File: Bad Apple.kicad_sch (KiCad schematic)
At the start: 0 parts

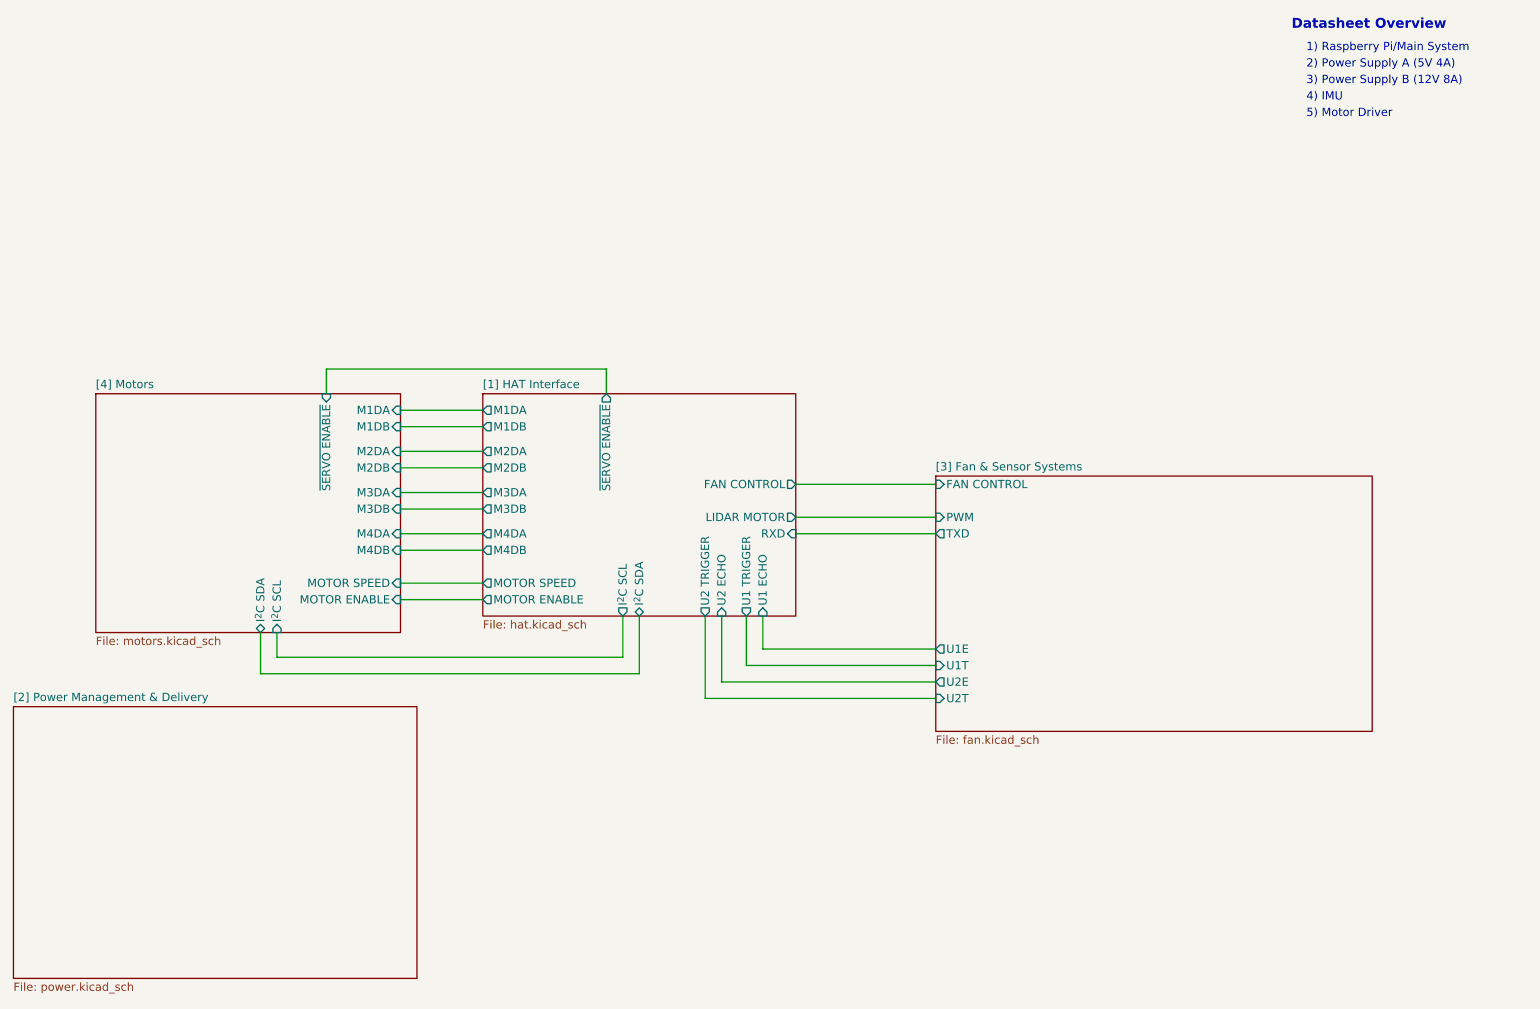
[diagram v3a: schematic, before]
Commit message: feat(pcb): (somewhat) finalized all the parts needed
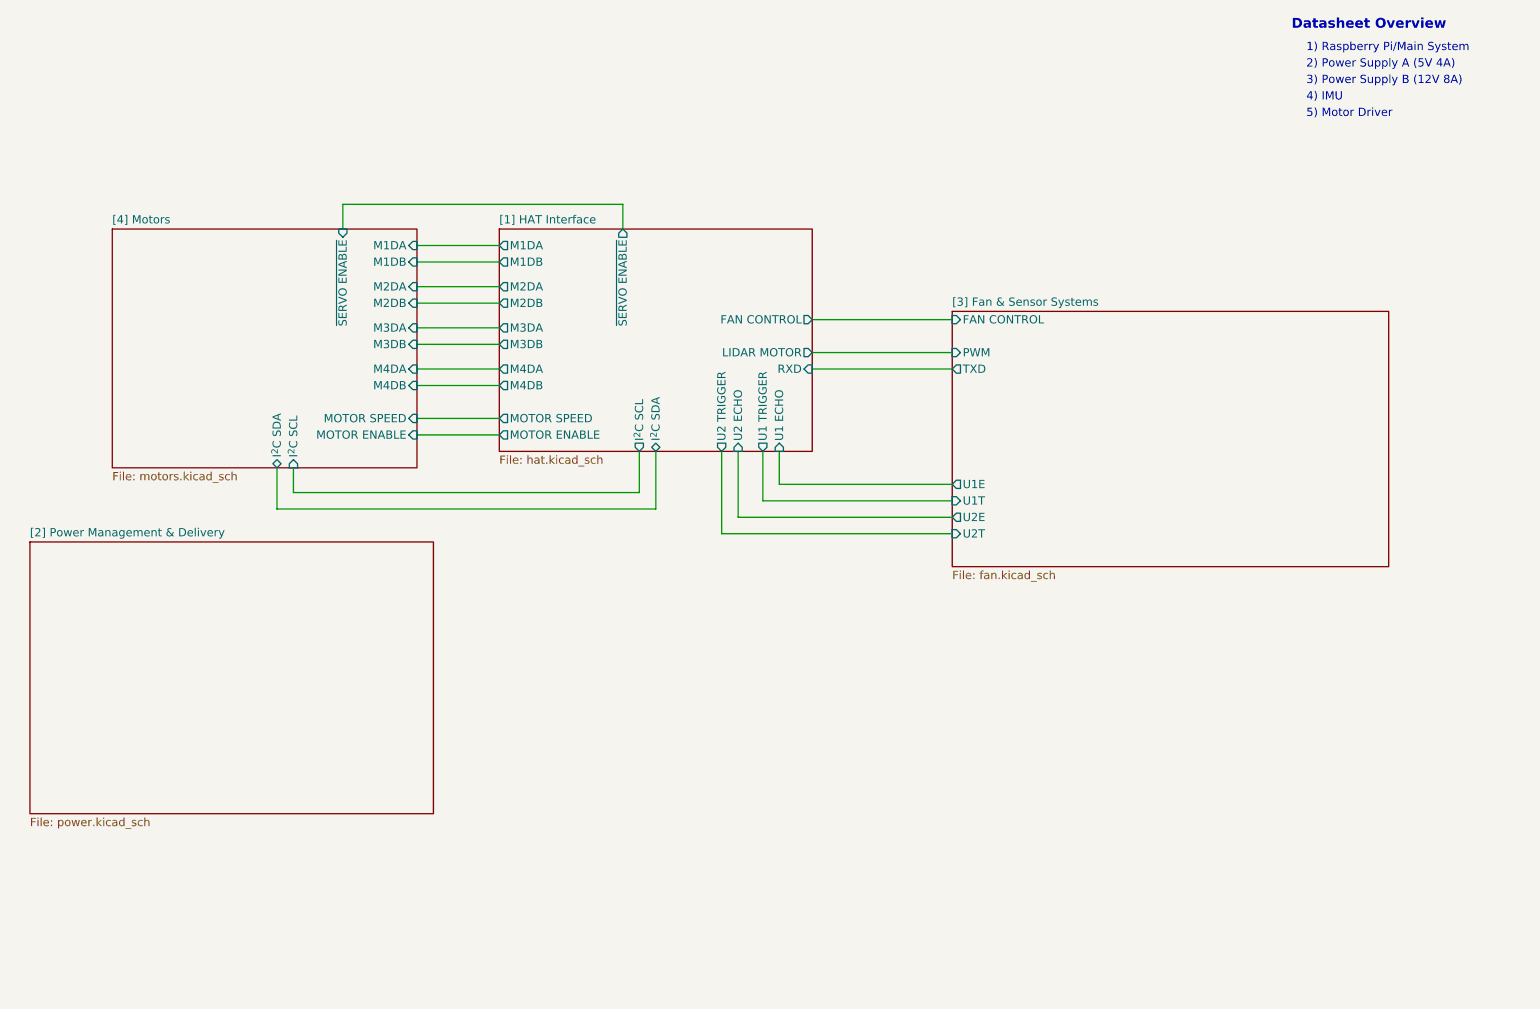
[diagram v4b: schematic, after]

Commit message: feat: cleared the PCB design for a much better thingy
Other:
- sheet [3] Fan & Sensor Systems ports: added I^{2}C SCL, I^{2}C SDA; removed none
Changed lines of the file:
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@@
+		)
+	)
+	(junction
+		(at 137.16 87.63)
+		(diameter 0)
+		(color 0 0 0 0)
+	)
+	(junction
+		(at 139.7 90.17)
+		(diameter 0)
+		(color 0 0 0 0)
+	)
+	(wire
+		(pts
+			(xy 212.09 99.06) (xy 212.09 107.95)
+		)
+		(stroke
+			(width 0)
+			(type default)
 		)
 	)
@@
 	(wire
 		(pts
+			(xy 209.55 105.41) (xy 139.7 105.41)
+		)
+		(stroke
+			(width 0)
+			(type default)
+		)
+	)
+	(wire
+		(pts
 			(xy 158.75 81.28) (xy 158.75 86.36)
 		)
@@
 	(wire
 		(pts
+			(xy 139.7 90.17) (xy 139.7 105.41)
+		)
+		(stroke
+			(width 0)
+			(type default)
+		)
+	)
+	(wire
+		(pts
+			(xy 212.09 107.95) (xy 137.16 107.95)
+		)
+		(stroke
+			(width 0)
+			(type default)
+		)
+	)
+	(wire
+		(pts
 			(xy 163.83 66.04) (xy 185.42 66.04)
 		)
@@
 	(wire
 		(pts
+			(xy 209.55 99.06) (xy 209.55 105.41)
+		)
+		(stroke
+			(width 0)
+			(type default)
+		)
+	)
+	(wire
+		(pts
 			(xy 102.87 49.53) (xy 115.57 49.53)
 		)
@@
 		(pts
 			(xy 102.87 64.77) (xy 115.57 64.77)
+		)
+		(stroke
+			(width 0)
+			(type default)
+		)
+	)
+	(wire
+		(pts
+			(xy 137.16 87.63) (xy 137.16 107.95)
 		)
 		(stroke
@@
 			(effects
 				(font
+					(size 1.27 1.27)
+				)
+				(justify left)
+			)
+		)
+		(pin "I^{2}C SCL" input
+			(at 212.09 99.06 270)
+			(effects
+				(font
+					(size 1.27 1.27)
+				)
+				(justify left)
+			)
+		)
+		(pin "I^{2}C SDA" bidirectional
+			(at 209.55 99.06 270)
+			(effects
+				(font

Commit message: feat: (hopefully) gave connections to everything else
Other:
- sheet [1] HAT Interface ports: added AUDIO CLK, AUDIO FRAME, AUDIO IN, AUDIO OUT; removed none
- sheet [3] Fan & Sensor Systems ports: added AUDIO CLK, AUDIO FRAME, AUDIO IN, AUDIO OUT; removed none
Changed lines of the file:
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@@
+	(wire
+		(pts
+			(xy 215.9 57.15) (xy 215.9 59.69)
+		)
+		(stroke
+			(width 0)
+			(type default)
+		)
+	)
 	(wire
 		(pts
@@
 	(wire
 		(pts
+			(xy 163.83 49.53) (xy 223.52 49.53)
+		)
+		(stroke
+			(width 0)
+			(type default)
+		)
+	)
+	(wire
+		(pts
+			(xy 220.98 59.69) (xy 220.98 52.07)
+		)
+		(stroke
+			(width 0)
+			(type default)
+		)
+	)
+	(wire
+		(pts
+			(xy 223.52 49.53) (xy 223.52 59.69)
+		)
+		(stroke
+			(width 0)
+			(type default)
+		)
+	)
+	(wire
+		(pts
+			(xy 163.83 57.15) (xy 215.9 57.15)
+		)
+		(stroke
+			(width 0)
+			(type default)
+		)
+	)
+	(wire
+		(pts
 			(xy 212.09 107.95) (xy 137.16 107.95)
 		)
@@
 	(wire
 		(pts
+			(xy 218.44 54.61) (xy 218.44 59.69)
+		)
+		(stroke
+			(width 0)
+			(type default)
+		)
+	)
+	(wire
+		(pts
 			(xy 91.44 46.99) (xy 91.44 43.18)
 		)
@@
 		(pts
 			(xy 156.21 81.28) (xy 156.21 88.9)
+		)
+		(stroke
+			(width 0)
+			(type default)
+		)
+	)
+	(wire
+		(pts
+			(xy 163.83 54.61) (xy 218.44 54.61)
+		)
+		(stroke
+			(width 0)
+			(type default)
+		)
+	)
+	(wire
+		(pts
+			(xy 220.98 52.07) (xy 163.83 52.07)
 		)
 		(stroke
@@
 			)
 		)
+		(pin "AUDIO CLK" output
+			(at 163.83 49.53 0)
+			(effects
+				(font
+					(size 1.27 1.27)
+				)
+				(justify right)
+			)
+		)
+		(pin "AUDIO FRAME" output
+			(at 163.83 52.07 0)
+			(effects
+				(font
+					(size 1.27 1.27)
+				)
+				(justify right)
+			)
+		)
+		(pin "AUDIO IN" input
+			(at 163.83 54.61 0)
+			(effects
+				(font
+					(size 1.27 1.27)
+				)
+				(justify right)
+			)
+		)
+		(pin "AUDIO OUT" output
+			(at 163.83 57.15 0)
+			(effects
+				(font
+					(size 1.27 1.27)
+				)
+				(justify right)
+			)
+		)
 		(instances
 			(project "Bad Apple"
@@
 			)
 		)
+		(pin "AUDIO CLK" input
+			(at 223.52 59.69 90)
+			(effects
+				(font
+					(size 1.27 1.27)
+				)
+				(justify right)
+			)
+		)
+		(pin "AUDIO FRAME" input
+			(at 220.98 59.69 90)
+			(effects
+				(font
+					(size 1.27 1.27)
+				)
+				(justify right)
+			)
+		)
+		(pin "AUDIO IN" output
+			(at 218.44 59.69 90)
+			(effects
+				(font
+					(size 1.27 1.27)
+				)
+				(justify right)
+			)
+		)
+		(pin "AUDIO OUT" input
+			(at 215.9 59.69 90)
+			(effects
+				(font
+					(size 1.27 1.27)
+				)
+				(justify right)
+			)
+		)

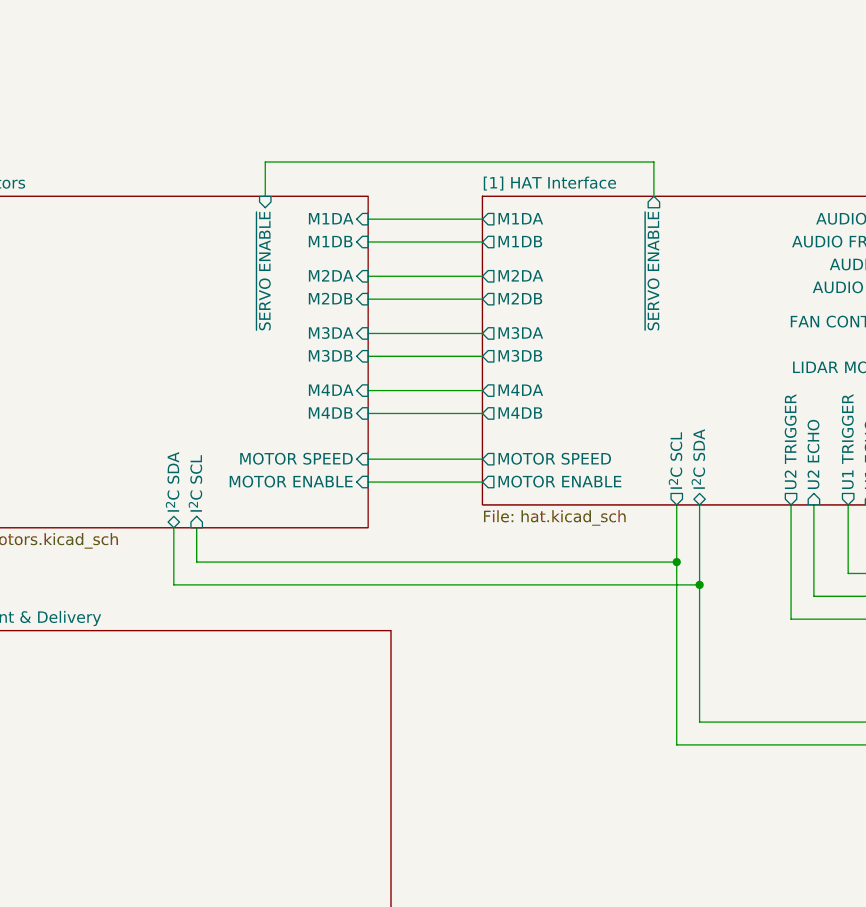
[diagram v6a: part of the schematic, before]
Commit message: feat: removed servo motors
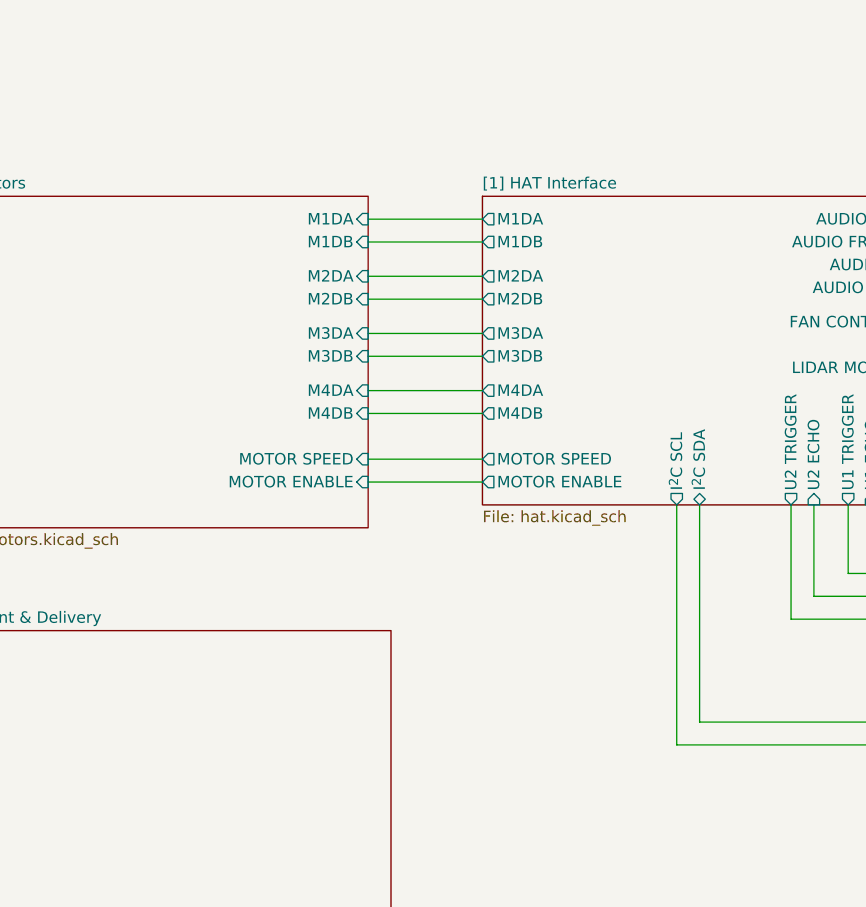
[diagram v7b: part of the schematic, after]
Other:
- sheet [1] HAT Interface ports: added none; removed ~{SERVO ENABLE}
- sheet [4] Motors ports: added none; removed I^{2}C SCL, I^{2}C SDA, ~{SERVO ENABLE}
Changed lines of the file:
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@@
 		)
-	)
-	(junction
-		(at 137.16 87.63)
-		(diameter 0)
-		(color 0 0 0 0)
-	)
-	(junction
-		(at 139.7 90.17)
-		(diameter 0)
-		(color 0 0 0 0)
 	)
 	(wire
@@
 	(wire
 		(pts
-			(xy 83.82 87.63) (xy 137.16 87.63)
-		)
-		(stroke
-			(width 0)
-			(type default)
-		)
-	)
-	(wire
-		(pts
-			(xy 139.7 90.17) (xy 81.28 90.17)
-		)
-		(stroke
-			(width 0)
-			(type default)
-		)
-	)
-	(wire
-		(pts
 			(xy 215.9 57.15) (xy 215.9 59.69)
 		)
@@
 	(wire
 		(pts
-			(xy 91.44 43.18) (xy 134.62 43.18)
-		)
-		(stroke
-			(width 0)
-			(type default)
-		)
-	)
-	(wire
-		(pts
 			(xy 209.55 105.41) (xy 139.7 105.41)
 		)
@@
 	(wire
 		(pts
-			(xy 137.16 81.28) (xy 137.16 87.63)
-		)
-		(stroke
-			(width 0)
-			(type default)
-		)
-	)
-	(wire
-		(pts
 			(xy 102.87 62.23) (xy 115.57 62.23)
 		)
@@
 	(wire
 		(pts
-			(xy 81.28 83.82) (xy 81.28 90.17)
-		)
-		(stroke
-			(width 0)
-			(type default)
-		)
-	)
-	(wire
-		(pts
 			(xy 163.83 68.58) (xy 185.42 68.58)
 		)
@@
 	(wire
 		(pts
-			(xy 139.7 90.17) (xy 139.7 105.41)
-		)
-		(stroke
-			(width 0)
-			(type default)
-		)
-	)
-	(wire
-		(pts
 			(xy 163.83 49.53) (xy 223.52 49.53)
 		)
@@
 	(wire
 		(pts
-			(xy 137.16 87.63) (xy 137.16 107.95)
+			(xy 137.16 81.28) (xy 137.16 107.95)
 		)
 		(stroke
@@
 	(wire
 		(pts
-			(xy 134.62 43.18) (xy 134.62 46.99)
-		)
-		(stroke
-			(width 0)
-			(type default)
-		)
-	)
-	(wire
-		(pts
 			(xy 163.83 60.96) (xy 185.42 60.96)
 		)
@@
 	(wire
 		(pts
-			(xy 139.7 81.28) (xy 139.7 90.17)
+			(xy 139.7 81.28) (xy 139.7 105.41)
 		)
 		(stroke
@@
 	(wire
 		(pts
-			(xy 91.44 46.99) (xy 91.44 43.18)
-		)
-		(stroke
-			(width 0)
-			(type default)
-		)
-	)
-	(wire
-		(pts
 			(xy 156.21 81.28) (xy 156.21 88.9)
 		)
@@
 		(pts
 			(xy 102.87 52.07) (xy 115.57 52.07)
-		)
-		(stroke
-			(width 0)
-			(type default)
-		)
-	)
-	(wire
-		(pts
-			(xy 83.82 83.82) (xy 83.82 87.63)
 		)
 		(stroke
@@
 			)
 		)
-		(pin "~{SERVO ENABLE}" output
-			(at 134.62 46.99 90)
-			(effects
-				(font
-					(size 1.27 1.27)
-				)
-				(justify right)
-			)
-		)
 		(pin "MOTOR ENABLE" output
 			(at 115.57 78.74 180)
@@
 			(effects
 				(font
-					(size 1.27 1.27)
-				)
-				(justify right)
-			)
-		)
-		(pin "I^{2}C SCL" input
-			(at 83.82 83.82 270)
-			(effects
-				(font
-					(size 1.27 1.27)
-				)
-				(justify left)
-			)
-		)
-		(pin "I^{2}C SDA" bidirectional
-			(at 81.28 83.82 270)
-			(effects
-				(font
-					(size 1.27 1.27)
-				)
-				(justify left)
-			)
-		)
-		(pin "~{SERVO ENABLE}" input
-			(at 91.44 46.99 90)
-			(effects
-				(font

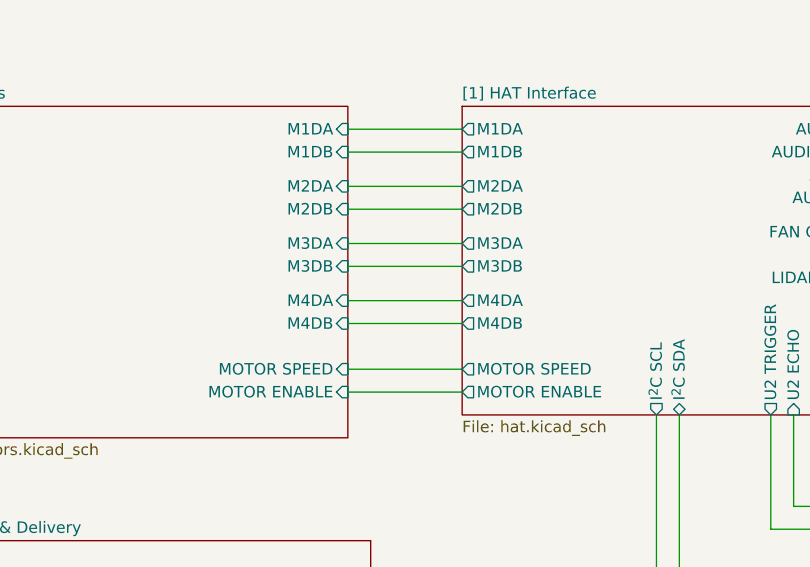
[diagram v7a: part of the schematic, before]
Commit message: feat: wired up audio system
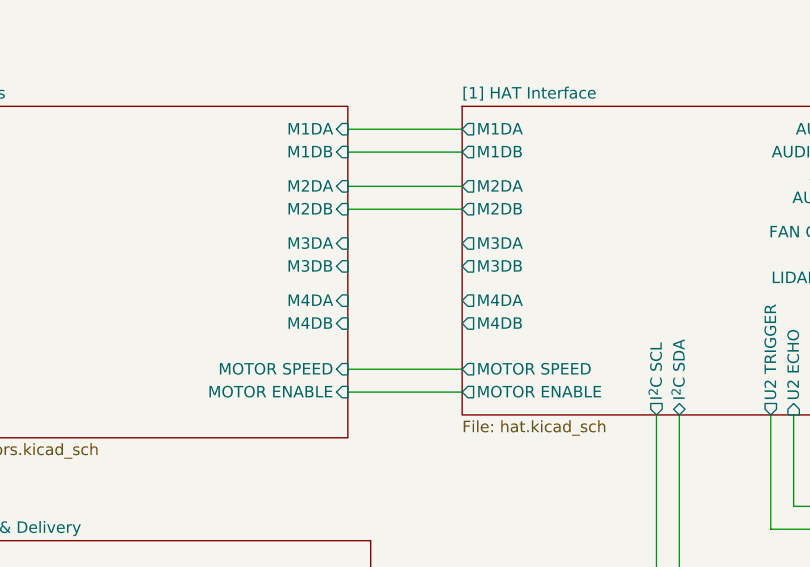
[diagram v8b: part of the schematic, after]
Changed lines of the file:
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@@
-	(wire
-		(pts
-			(xy 102.87 62.23) (xy 115.57 62.23)
-		)
-		(stroke
-			(width 0)
-			(type default)
-		)
-	)
 	(wire
 		(pts
@@
 	(wire
 		(pts
-			(xy 102.87 64.77) (xy 115.57 64.77)
-		)
-		(stroke
-			(width 0)
-			(type default)
-		)
-	)
-	(wire
-		(pts
 			(xy 137.16 81.28) (xy 137.16 107.95)
-		)
-		(stroke
-			(width 0)
-			(type default)
-		)
-	)
-	(wire
-		(pts
-			(xy 102.87 68.58) (xy 115.57 68.58)
 		)
 		(stroke
@@
 		)
 		(stroke
-			(width 0)
-			(type default)
-		)
-	)
-	(wire
-		(pts
-			(xy 102.87 71.12) (xy 115.57 71.12)
-		)
-		(stroke
